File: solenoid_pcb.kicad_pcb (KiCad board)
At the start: 2 copper layers, 22.5 x 22.5 mm, 23 parts, among them J1 Power, J2 PGM, J3 Solenoid, SW1 RESET, U1 TPS561201, U2 ESP-12F, U3 MCP14A0305xMNY

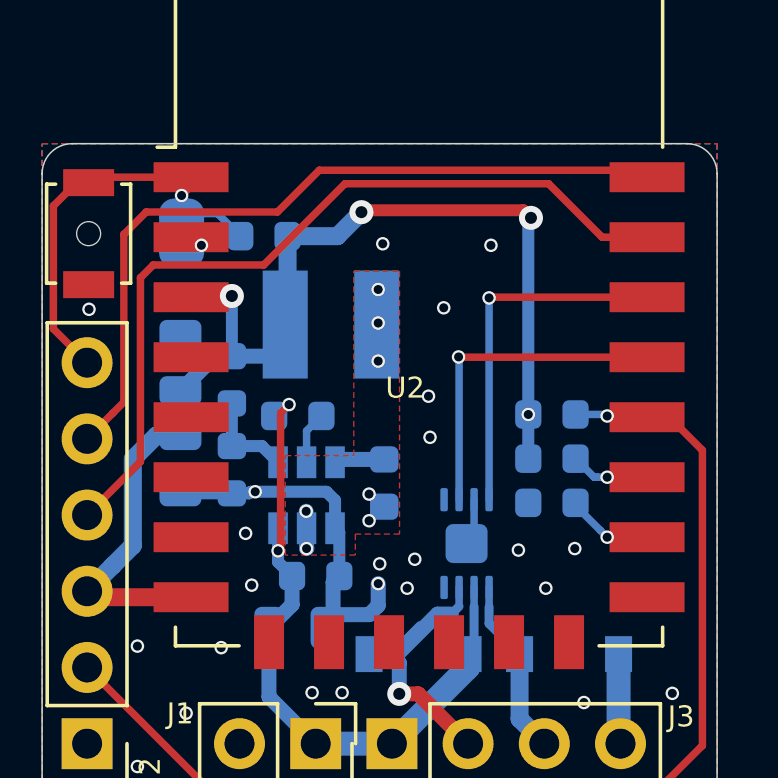
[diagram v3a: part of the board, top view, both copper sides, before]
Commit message: Apply real small routing update (gnd via's)
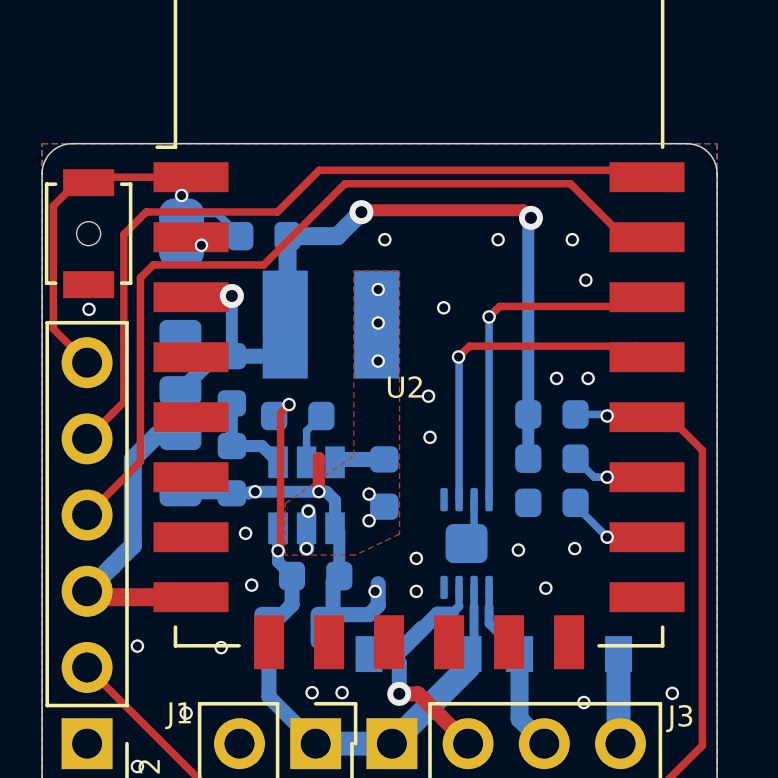
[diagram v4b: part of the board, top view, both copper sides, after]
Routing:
- net GND: track 17.4 -> 18.5 mm, vias 25 -> 29
- net +3V3: vias 4 -> 3
